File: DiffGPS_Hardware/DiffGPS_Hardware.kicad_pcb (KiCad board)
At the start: 2 copper layers, 110.2 x 72.3 mm, 16 parts, among them U1 Raspberry_Pi

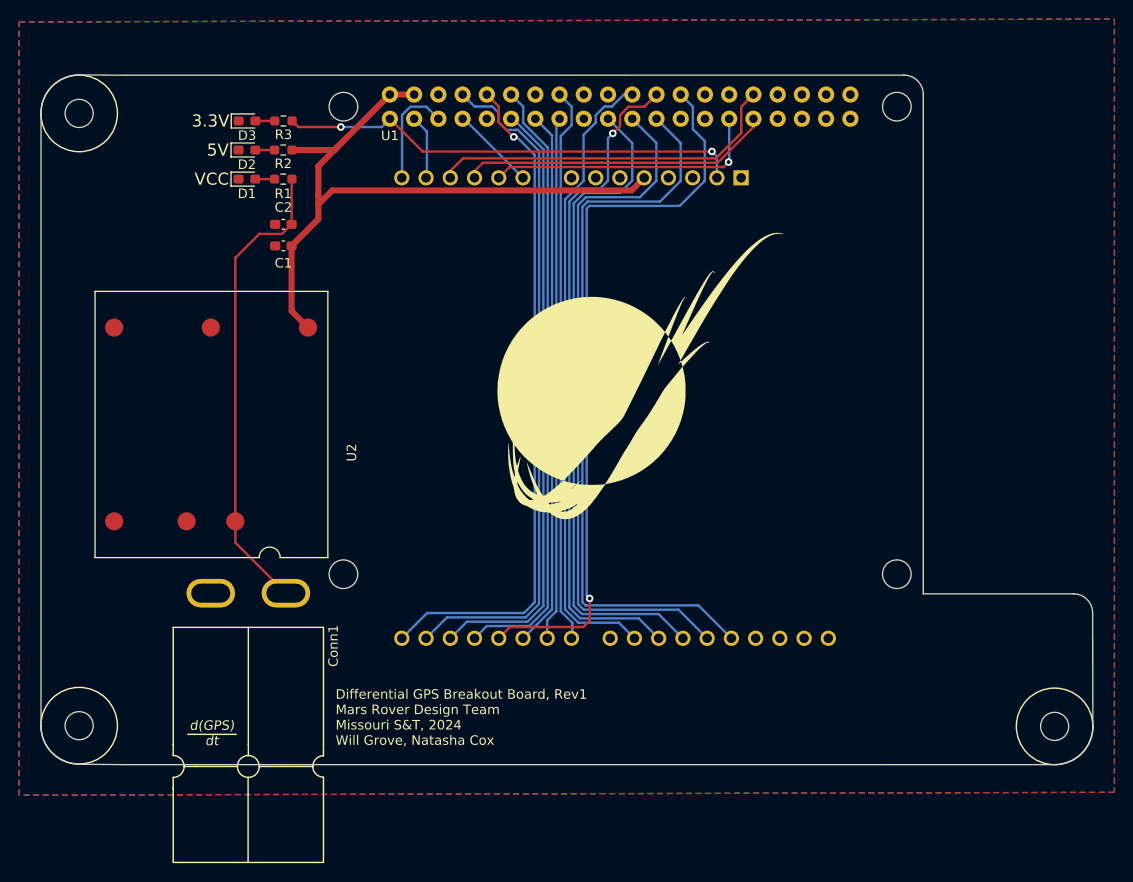
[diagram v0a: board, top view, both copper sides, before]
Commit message: updated Pi symbol, fixed various things
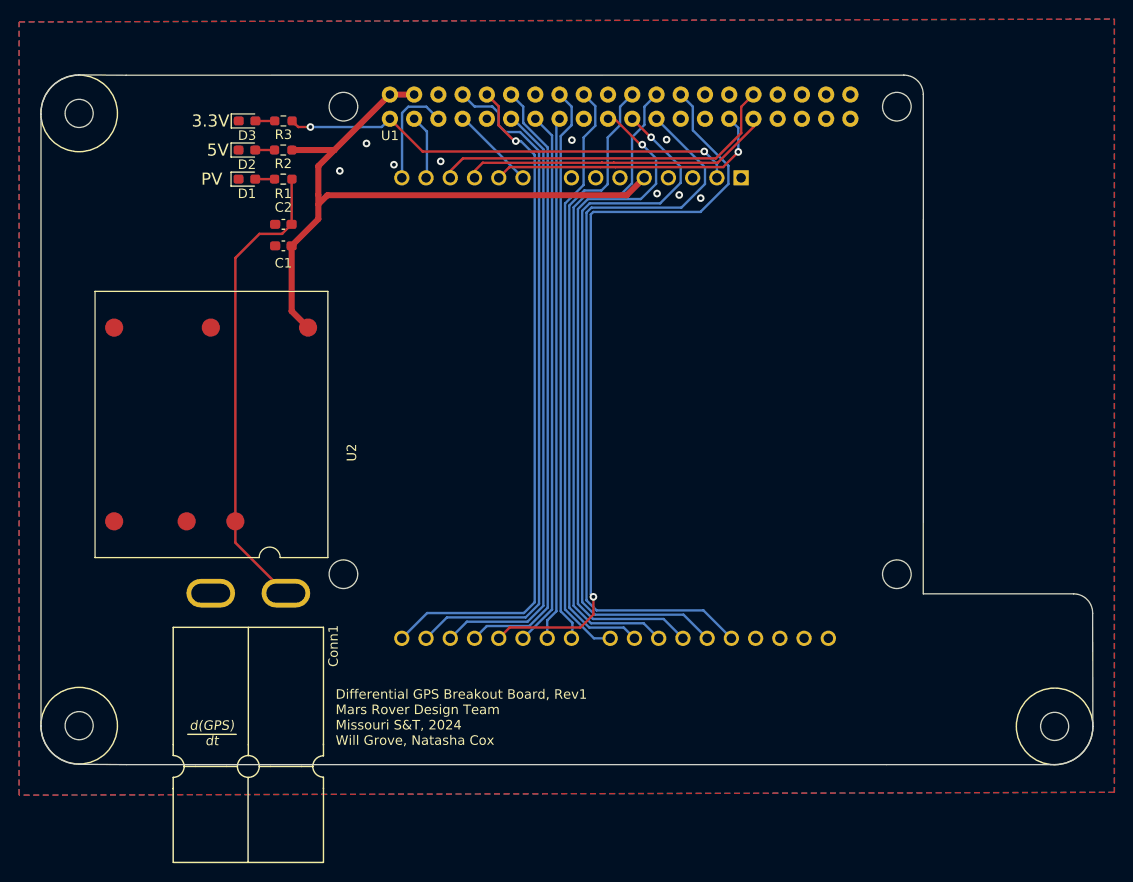
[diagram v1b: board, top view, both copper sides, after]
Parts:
- removed G***: LOGO, MRDT_Silkscreens:0_MRDT_Logo_30mm
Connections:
- U1 pad 18: (no net) -> D8
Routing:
- net D8: track 0.00 -> 61.8 mm
- net D4: track 77.3 -> 80.2 mm
- net D11: track 69.7 -> 72.6 mm, vias 0 -> 1
- net D13: track 77.6 -> 80.1 mm
- net D12: track 73.6 -> 76.0 mm, vias 0 -> 1
- net A1: track 29.3 -> 30.1 mm
- net D10: track 70.3 -> 69.6 mm, vias 1 -> 0
- net D9: track 66.4 -> 65.7 mm
- net GND: vias 0 -> 9
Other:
- board text added: "PV"
- board text removed: "VCC"

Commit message: minor changes
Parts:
- added G***: LOGO, MRDT_Silkscreens:0_MRDT_Logo_40mm, F.Cu at (107.6, 74.9)
- moved H2 11.8 mm to (53.9, 50.6), turned to 90 degrees
- moved H1 0.06 mm to (45.9, 114.2)
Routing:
- net +5V: track 71.7 -> 72.3 mm
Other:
- outline, holes or cut-outs redrawn

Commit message: finished GERBS
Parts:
- moved H3 0.41 mm to (155.7, 114.2)
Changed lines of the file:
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@@
       (drillshape 0)
       (scaleselection 1)
-      (outputdirectory "../Manufacturing/")
+      (outputdirectory "../Manufacturing/Gerbs/")
     )
   )
@@
   )
   (footprint "MRDT_Drill_Holes:4_40_Hole_Corner" (layer "F.Cu")
-    (at 156.0757 114.3 90)
+    (at 155.6653 114.24412 90)
     (property "Sheetfile" "DiffGPS_Hardware.kicad_sch")
     (property "Sheetname" "")

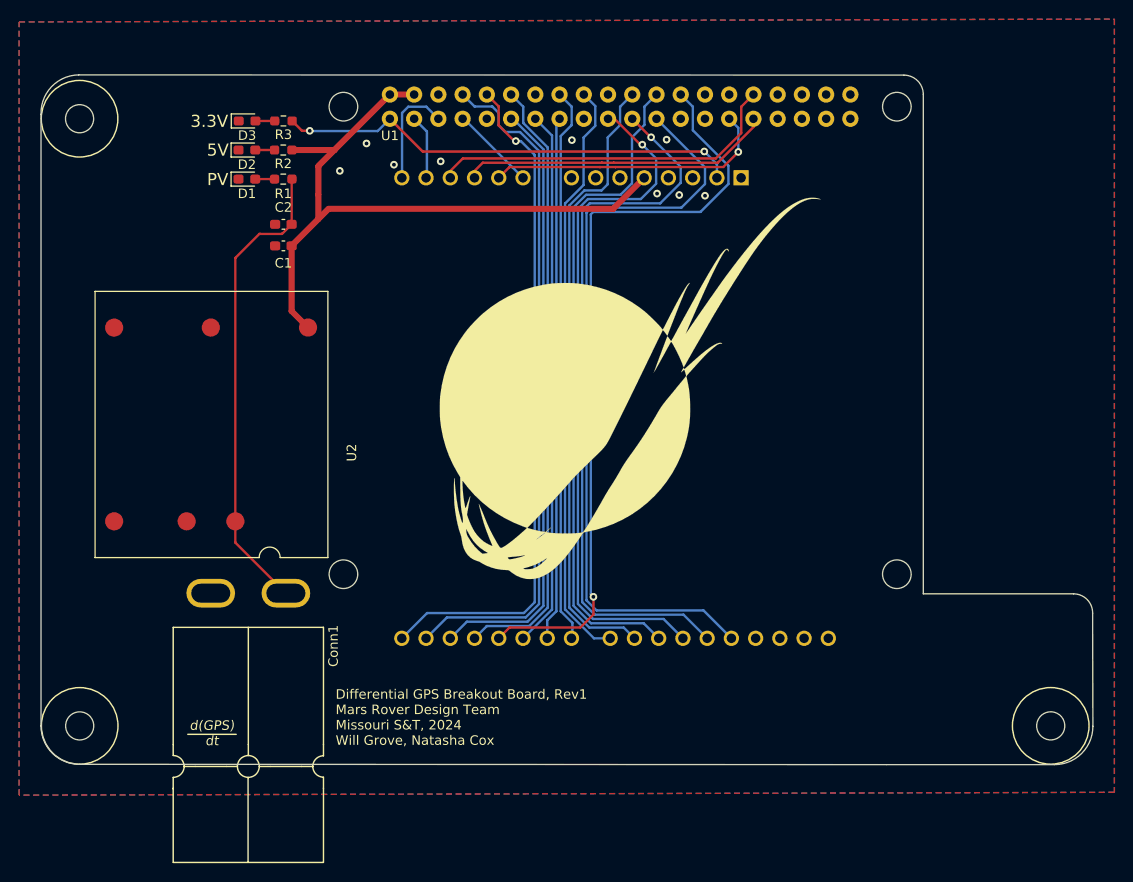
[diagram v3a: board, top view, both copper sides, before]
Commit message: Changed and moved capacitor
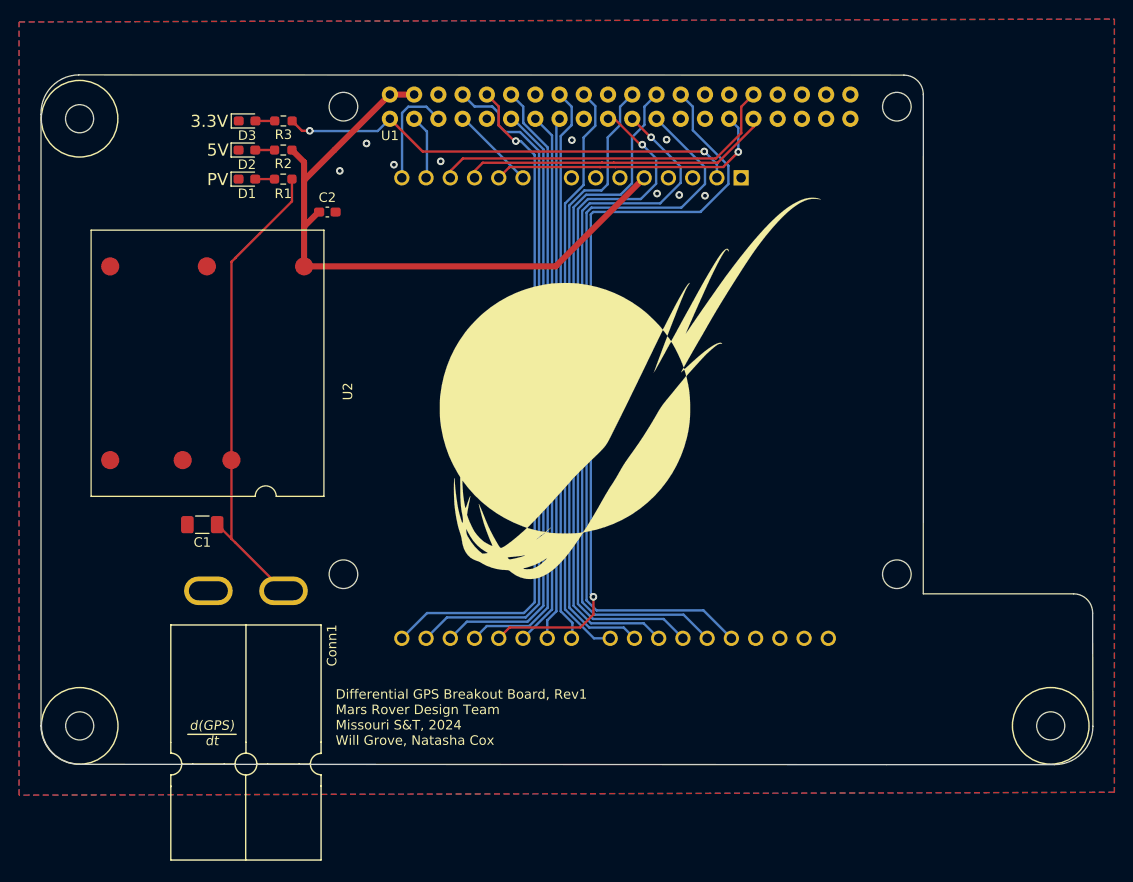
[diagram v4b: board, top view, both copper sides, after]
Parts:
- C1: footprint Capacitor_SMD:C_0603_1608Metric_Pad1.08x0.95mm_HandSolder -> Capacitor_SMD:C_1206_3216Metric_Pad1.33x1.80mm_HandSolder
- Conn1: footprint MRDT_Connectors:Square_Anderson_2_H_Side_By_Side -> MRDT_Connectors:Square_Anderson_2_H_Side_By_Side_PV
- moved C1 32.6 mm to (62.7, 89.2)
- moved U2 6.43 mm to (78.5, 75.2)
- moved C2 5.81 mm to (75.8, 56.4), turned to 180 degrees
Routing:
- net +5V: track 72.3 -> 69.7 mm
- net VCC: track 49.4 -> 50.6 mm
